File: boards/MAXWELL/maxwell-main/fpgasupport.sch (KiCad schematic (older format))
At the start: 43 parts, among them J10 XILINX_JTAG, U2 XC7K160T-2FFG676C, U34 S25FL128LAGNFV010

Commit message: Began assigning IC footprints
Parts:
- U2: footprint (none) -> azonenberg_pcb:BGA_676_27x27_FULLARRAY_1MM_FFG676
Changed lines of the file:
@@
 F 0 "U2" H 8350 4850 50  0000 L CNN
 F 1 "XC7K160T-2FFG676C" H 8350 4750 50  0000 L CNN
-F 2 "" H 8350 4900 50  0001 C CNN
+F 2 "azonenberg_pcb:BGA_676_27x27_FULLARRAY_1MM_FFG676" H 8350 4900 50  0001 C CNN
 F 3 "" H 8350 4900 50  0001 C CNN
 	1    8350 4900
@@
 F 0 "U2" H 4500 6500 50  0000 L CNN
 F 1 "XC7K160T-2FFG676C" H 4500 6400 50  0000 L CNN
-F 2 "" H 4500 6550 50  0001 C CNN
+F 2 "azonenberg_pcb:BGA_676_27x27_FULLARRAY_1MM_FFG676" H 4500 6550 50  0001 C CNN
 F 3 "" H 4500 6550 50  0001 C CNN
 	2    4500 6550
@@
 F 0 "U2" H 1600 6800 50  0000 L CNN
 F 1 "XC7K160T-2FFG676C" H 1600 6700 50  0000 L CNN
-F 2 "" H 1600 6850 50  0001 C CNN
+F 2 "azonenberg_pcb:BGA_676_27x27_FULLARRAY_1MM_FFG676" H 1600 6850 50  0001 C CNN
 F 3 "" H 1600 6850 50  0001 C CNN
 	3    1600 6850

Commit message: Added footprints for most ICs other than DC-DC modules
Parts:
- U34: footprint (none) -> azonenberg_pcb:DFN_8_1.27MM_6x5MM
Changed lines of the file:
@@
 F 0 "U34" H 13500 2587 60  0000 C CNN
 F 1 "S25FL128LAGNFV010" H 13500 2481 60  0000 C CNN
-F 2 "" H 13500 1900 60  0001 C CNN
+F 2 "azonenberg_pcb:DFN_8_1.27MM_6x5MM" H 13500 1900 60  0001 C CNN
 F 3 "" H 13500 1900 60  0000 C CNN
 	1    13500 1900

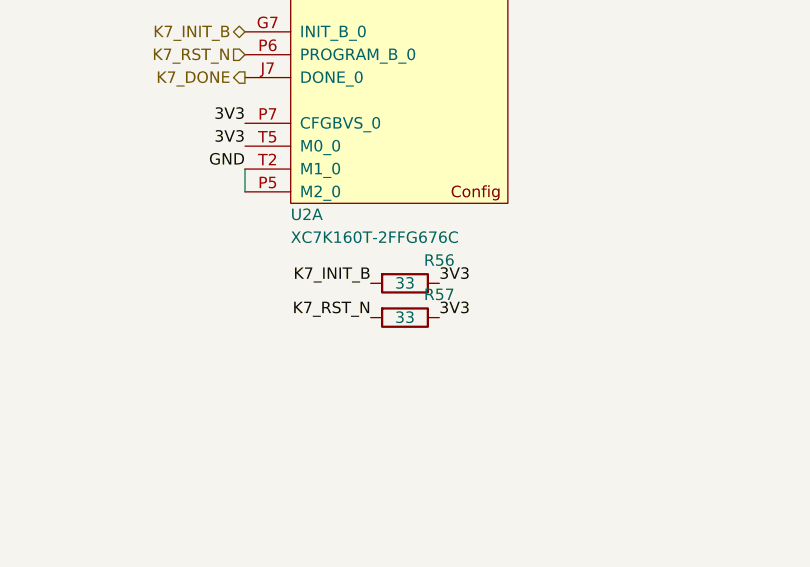
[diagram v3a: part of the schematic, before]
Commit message: Fixed bad pullup value on Kintex INIT_B
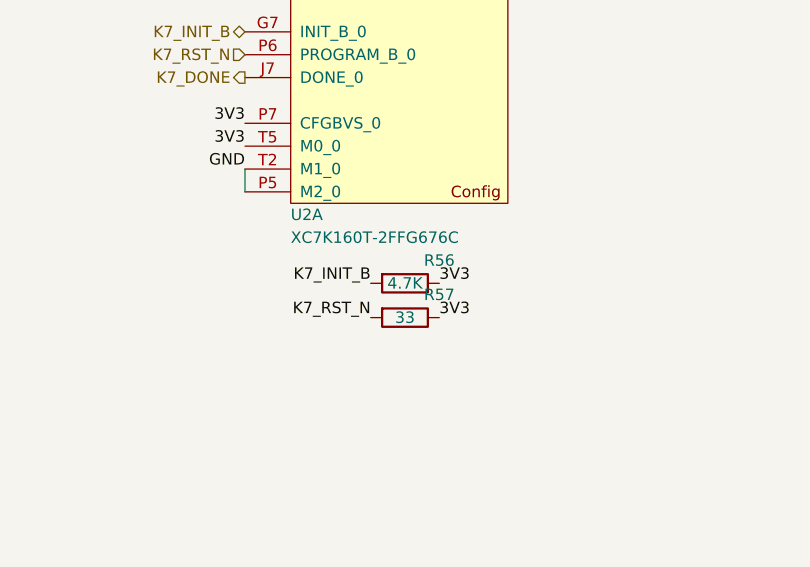
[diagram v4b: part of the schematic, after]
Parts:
- R56: value 33 -> 4.7K
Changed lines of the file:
@@
 P 8850 5250
 F 0 "R56" V 8750 5400 50  0000 C CNN
-F 1 "33" V 8850 5250 50  0000 C CNN
+F 1 "4.7K" V 8850 5250 50  0000 C CNN
 F 2 "azonenberg_pcb:EIA_0402_RES_NOSILK" V 8780 5250 50  0001 C CNN
 F 3 "" H 8850 5250 50  0001 C CNN

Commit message: Continued schematic review
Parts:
- added R245, R246, R247: 4.7K, azonenberg_pcb:EIA_0402_RES_NOSILK, symbol device:R
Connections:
- net 3V3: now also R245.1, R246.1, R247.1
- net K7_QSPI_CS_N: now also R245.2
- net K7_QSPI_DQ2: now also R246.2
- net K7_QSPI_DQ3: now also R247.2
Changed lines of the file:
@@
 Sheet 18 18
 Title "MAXWELL Main Board"
-Date "2020-06-24"
+Date "2020-06-25"
 Rev "0.1"
 Comp "Antikernel Labs"
@@
 U 1 1 5FEE98C8
 P 8850 5250
-F 0 "R56" V 8750 5400 50  0000 C CNN
+F 0 "R56" V 8800 5450 50  0000 C CNN
 F 1 "4.7K" V 8850 5250 50  0000 C CNN
 F 2 "azonenberg_pcb:EIA_0402_RES_NOSILK" V 8780 5250 50  0001 C CNN
@@
 Text Label 8700 5250 2    50   ~ 0
 K7_INIT_B
-Text Label 9000 5250 0    50   ~ 0
+Text Label 9300 5250 0    50   ~ 0
 3V3
 $Comp
@@
 U 1 1 5FEECA55
 P 8850 5400
-F 0 "R57" V 8750 5550 50  0000 C CNN
+F 0 "R57" V 8800 5600 50  0000 C CNN
 F 1 "33" V 8850 5400 50  0000 C CNN
 F 2 "azonenberg_pcb:EIA_0402_RES_NOSILK" V 8780 5400 50  0001 C CNN
@@
 Text Label 8700 5400 2    50   ~ 0
 K7_RST_N
-Text Label 9000 5400 0    50   ~ 0
-3V3
 $Comp
 L device:C C164
@@
 Wire Wire Line
 	3000 800  3000 1000
+$Comp
+L device:R R245
+U 1 1 62C5B6A4
+P 8850 5550
+F 0 "R245" V 8800 5700 50  0000 C CNN
+F 1 "4.7K" V 8850 5550 50  0000 C CNN
+F 2 "azonenberg_pcb:EIA_0402_RES_NOSILK" V 8780 5550 50  0001 C CNN
+F 3 "" H 8850 5550 50  0001 C CNN
+	1    8850 5550
+	0    1    1    0
+$EndComp
+Text Label 8700 5550 2    50   ~ 0
+K7_QSPI_CS_N
+$Comp
+L device:R R246
+U 1 1 62C5D0A3
+P 8850 5700
+F 0 "R246" V 8800 5850 50  0000 C CNN
+F 1 "4.7K" V 8850 5700 50  0000 C CNN
+F 2 "azonenberg_pcb:EIA_0402_RES_NOSILK" V 8780 5700 50  0001 C CNN
+F 3 "" H 8850 5700 50  0001 C CNN
+	1    8850 5700
+	0    1    1    0
+$EndComp
+Text Label 8700 5700 2    50   ~ 0
+K7_QSPI_DQ2
+$Comp
+L device:R R247
+U 1 1 62C5D576
+P 8850 5850
+F 0 "R247" V 8800 6000 50  0000 C CNN
+F 1 "4.7K" V 8850 5850 50  0000 C CNN
+F 2 "azonenberg_pcb:EIA_0402_RES_NOSILK" V 8780 5850 50  0001 C CNN
+F 3 "" H 8850 5850 50  0001 C CNN
+	1    8850 5850
+	0    1    1    0
+$EndComp
+Text Label 8700 5850 2    50   ~ 0
+K7_QSPI_DQ3
+Wire Wire Line
+	9000 5850 9000 5700
+Wire Wire Line
+	9000 5250 9300 5250
+Connection ~ 9000 5250
+Connection ~ 9000 5400
+Wire Wire Line
+	9000 5400 9000 5250
+Connection ~ 9000 5550
+Wire Wire Line
+	9000 5550 9000 5400
+Connection ~ 9000 5700
+Wire Wire Line
+	9000 5700 9000 5550
 $EndSCHEMATC

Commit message: Finished design review!!
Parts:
- added TP57, TP58, TP59, TP60, TP61, TP62, TP63, TP64, TP65, TP66, TP67, TP68, TP69, TP70, TP71, TP72, TP73: TESTCLIP, azonenberg_pcb:TESTPOINT_SMT_KEYSTONE_5016, symbol Connector:Conn_01x01
- added TP74, TP75, TP76: TESTPAD, azonenberg_pcb:TESTPOINT_SMT_0.5MM, symbol Connector:Conn_01x01
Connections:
- net 1V0_1: now also TP57.1 (Pin_1)
- net 1V2: now also TP66.1 (Pin_1)
- net 1V5: now also TP60.1 (Pin_1)
- net 1V8: now also TP58.1 (Pin_1), TP67.1 (Pin_1)
- net 2V0: now also TP59.1 (Pin_1)
- net 2V5: now also TP62.1 (Pin_1)
- net 3V3: now also TP61.1 (Pin_1)
- net GND: now also TP68.1 (Pin_1), TP69.1 (Pin_1), TP70.1 (Pin_1), TP71.1 (Pin_1), TP72.1 (Pin_1), TP73.1 (Pin_1)
- net GTX_1V0: now also TP63.1 (Pin_1)
- net GTX_1V2: now also TP64.1 (Pin_1)
- net GTX_1V8: now also TP65.1 (Pin_1)
- net K7_DONE: now also TP76.1 (Pin_1)
- net K7_INIT_B: now also TP74.1 (Pin_1)
- net K7_RST_N: now also TP75.1 (Pin_1)
